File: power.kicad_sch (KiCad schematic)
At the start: 48 parts, among them J3 Barrel_Jack_Switch, Q10 RJK0355DSP, Q11 DMP3037LSS-13, Q8 2N7002, Q9 RJK0355DSP, U5 MIC2101, U6 NCP1117-3.3_SOT223

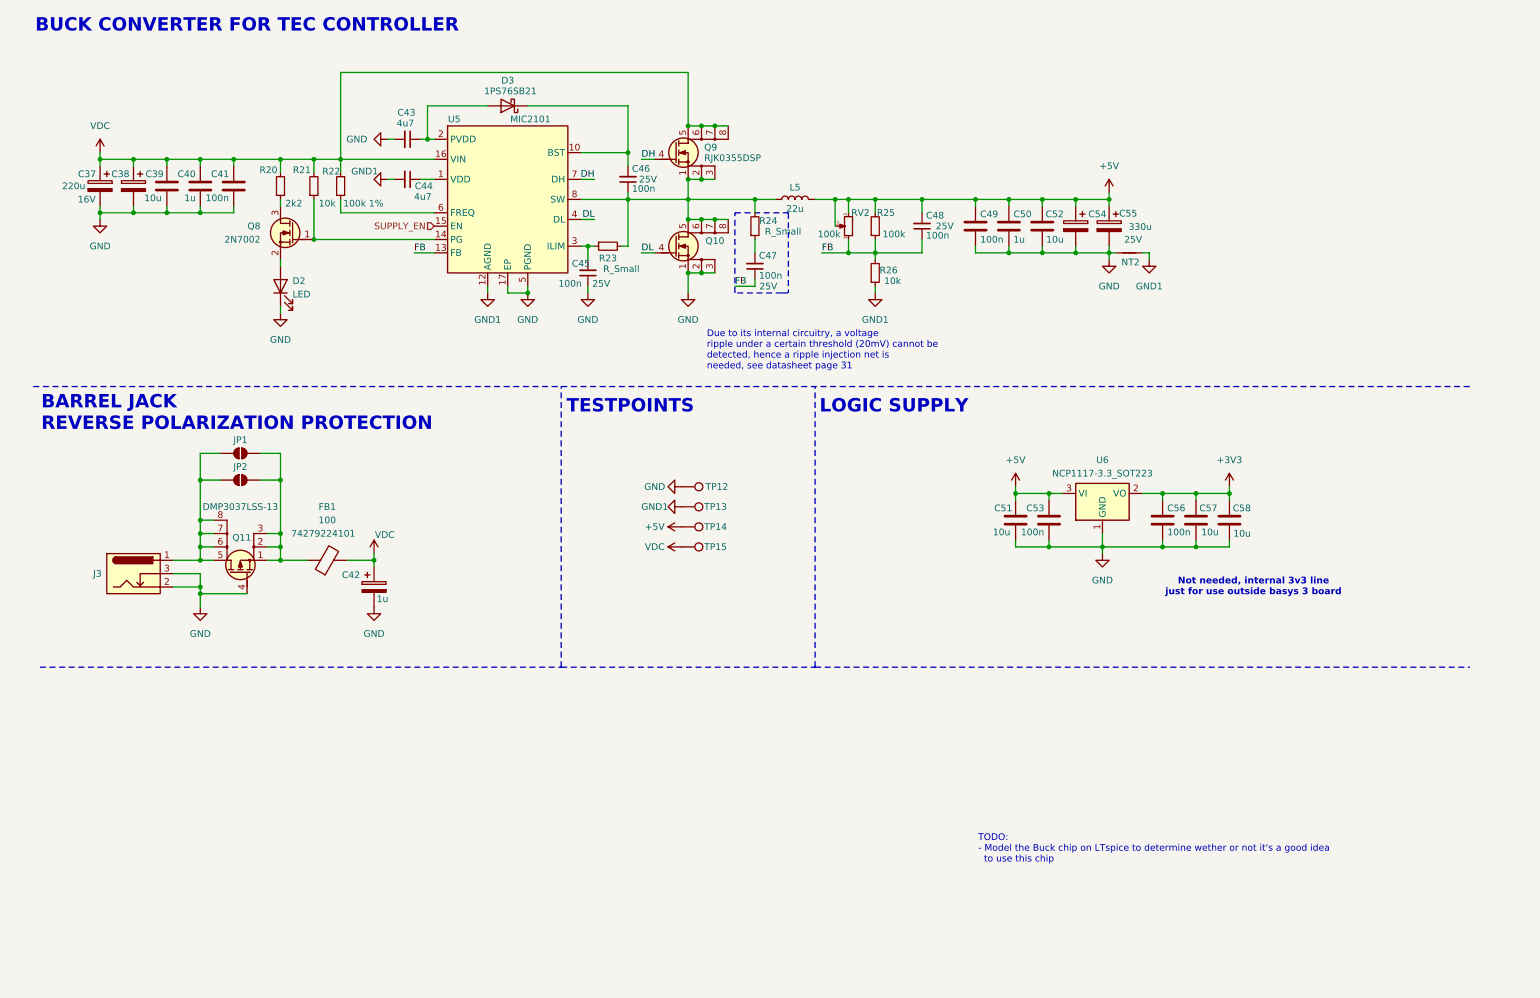
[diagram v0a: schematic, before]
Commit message: small schematic correction, structural changes to the 5V buck on the pcb
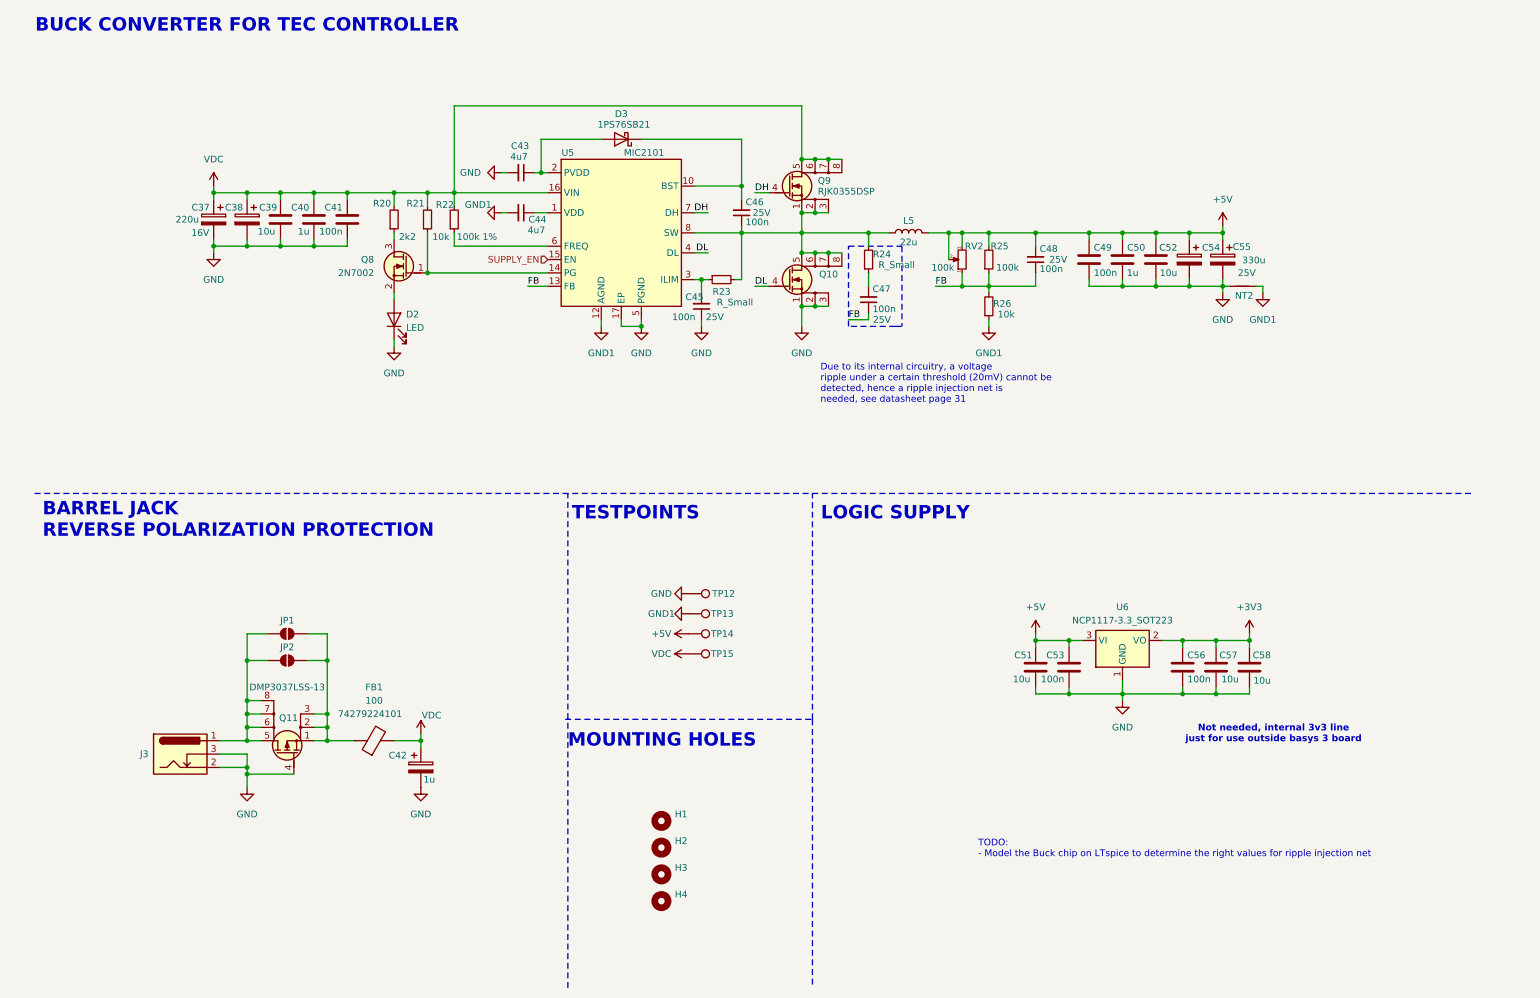
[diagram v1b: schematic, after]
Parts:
- added H1, H2, H3, H4: MountingHole, MountingHole:MountingHole_3.2mm_M3_ISO7380, symbol Mechanical:MountingHole
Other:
- note added: "MOUNTING HOLES"
- note added: "TODO: - Model the Buck chip on LTspice to determine the right values for ripple injection net"
- note removed: "TODO: - Model the Buck chip on LTspice to determine wether or not it's a good idea to use this chip"
- moved on the sheet: C37, C38, C39, C40, C41, C42, C43, C44, C45, C46, C47, C48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

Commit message: update PCB: fixed buck layout, concept layout for LD driver with LT3743
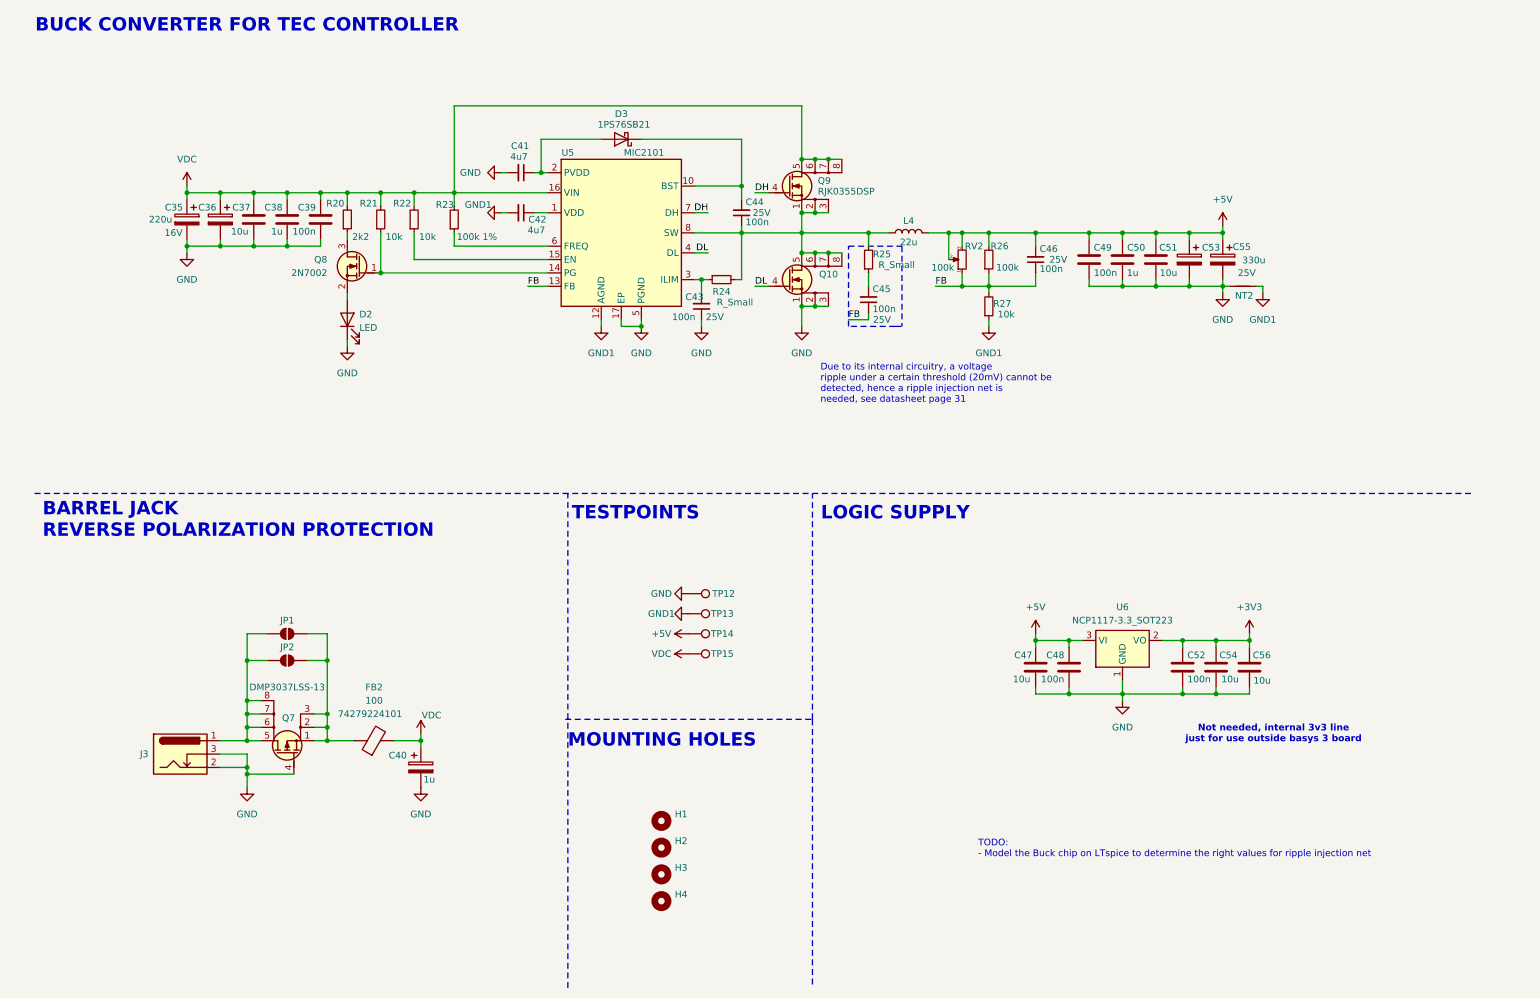
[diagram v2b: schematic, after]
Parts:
- added R22: 10k, Resistor_SMD:R_0603_1608Metric, symbol Device:R_Small
- TP13: footprint TestPoint:TestPoint_Pad_2.5x2.5mm -> TestPoint:TestPoint_Pad_1.0x1.0mm
- renumbered C37 to C35, C38 to C36, C39 to C37, C40 to C38, C41 to C39, C42 to C40, C43 to C41, C44 to C42, C45 to C43, C46 to C44, C47 to C45, C48 to C46, C51 to C47, C53 to C48, C52 to C51, C56 to C52, C54 to C53, C57 to C54, C58 to C56, FB1 to FB2, L5 to L4, Q11 to Q7, R22 to R23, R23 to R24, R24 to R25, R25 to R26, R26 to R27
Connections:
- net VDC: now also R22.2
- net SUPPLY_EN: no longer names the net of U5.15 (EN)
- net SUPPLY_EN: now also R22.1
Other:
- moved on the sheet: C35, C36, C37, C38, C39, D2, Q8, R20, R21

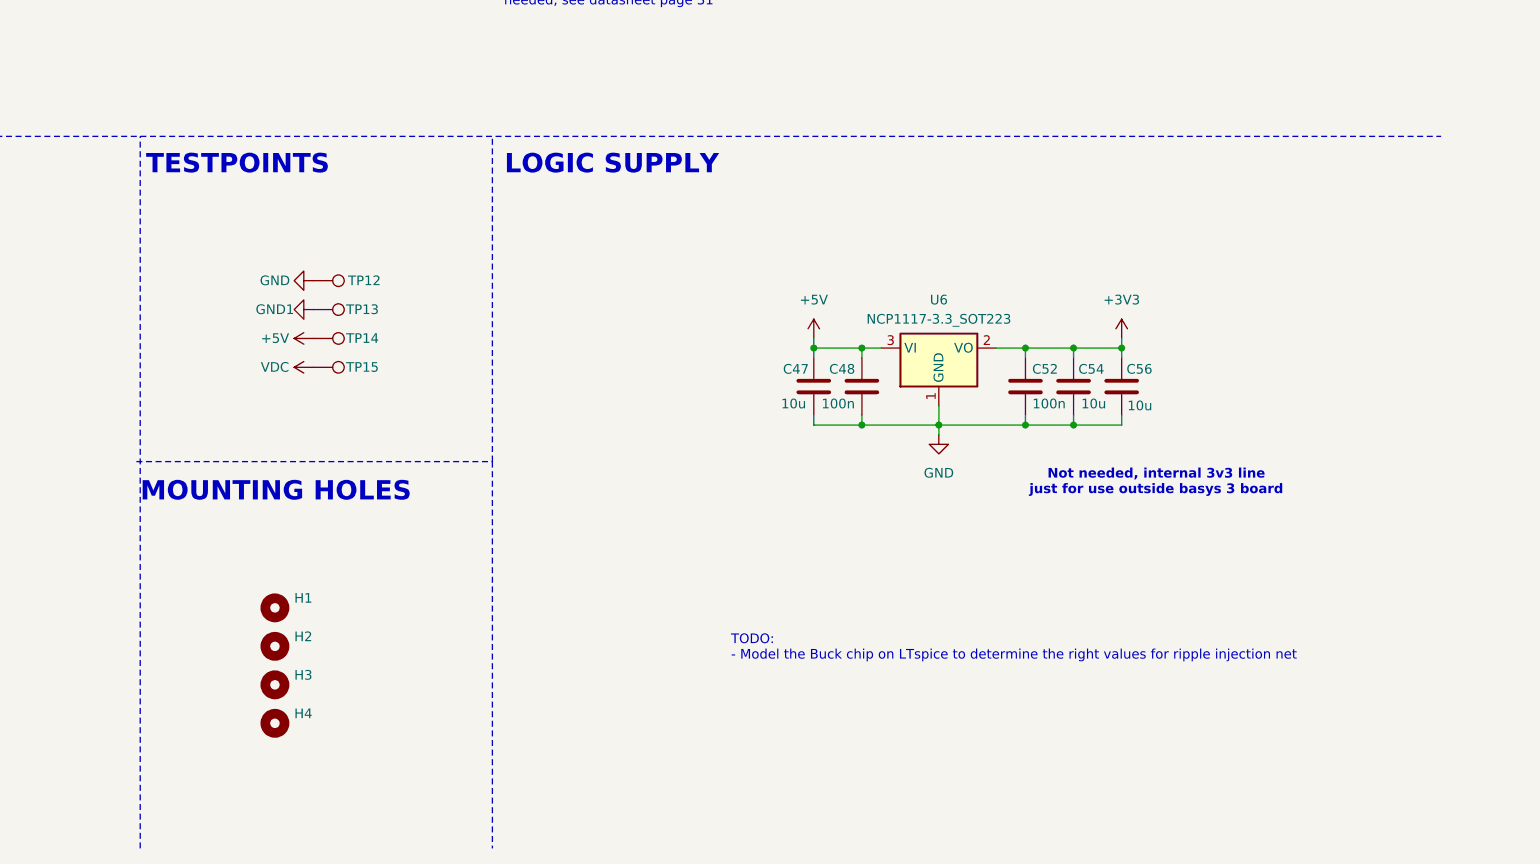
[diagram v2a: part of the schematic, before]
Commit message: Changed overall subsystem positions, TEC controller implemented, LD controller IC position to be reconsidered in order to have enough clearance after header connector is fully routed
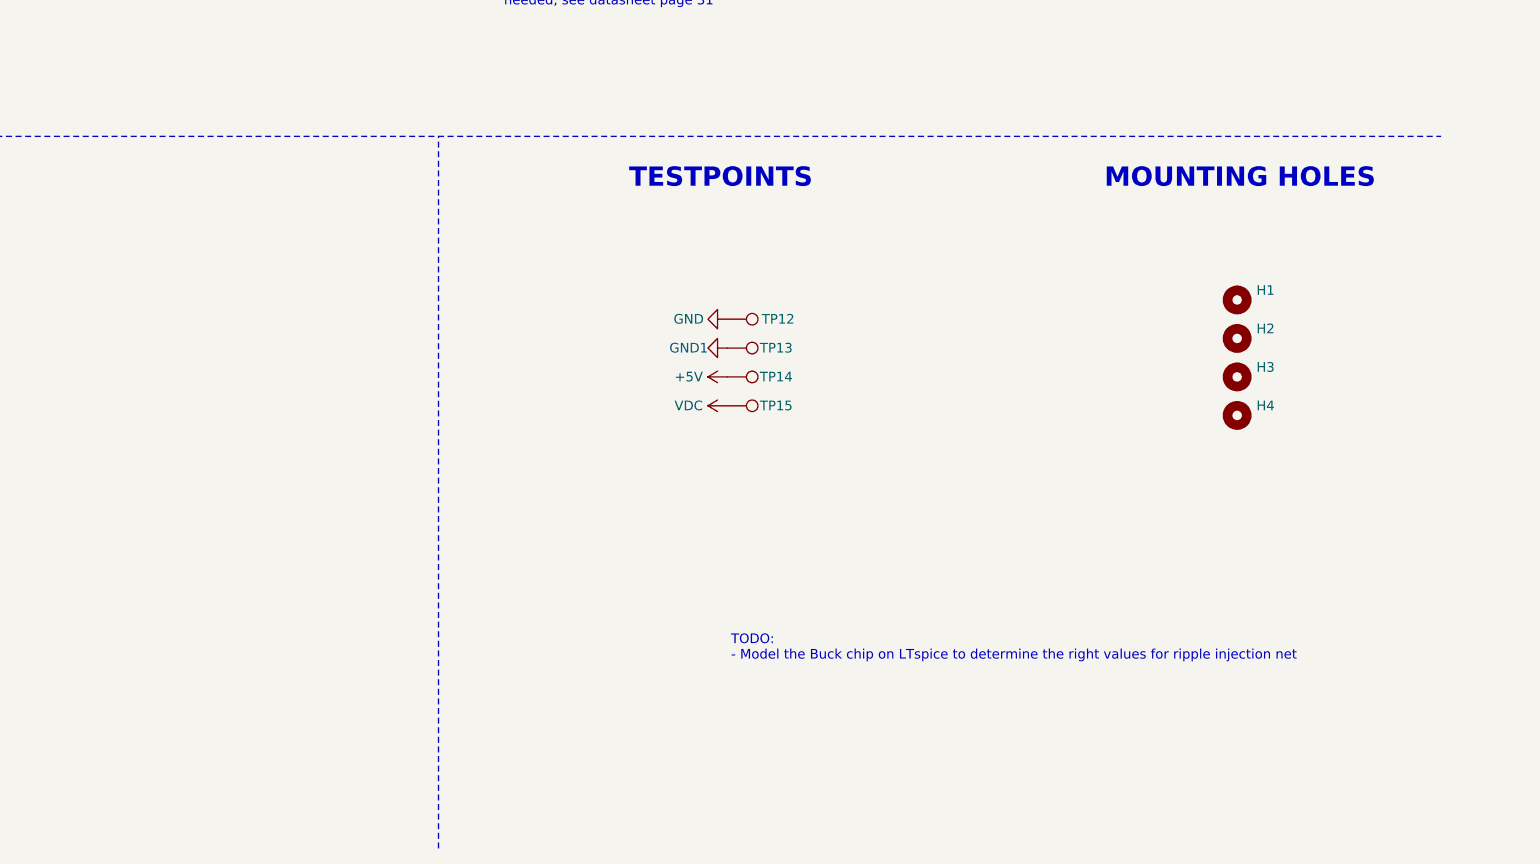
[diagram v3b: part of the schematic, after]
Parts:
- removed C47, C54, C56: 10u, Capacitor_SMD:C_0805_2012Metric, symbol Device:C
- removed C48, C52: 100n, Capacitor_SMD:C_0805_2012Metric, symbol Device:C
- removed U6: NCP1117-3.3_SOT223, Package_TO_SOT_SMD:SOT-223-3_TabPin2, symbol Regulator_Linear:NCP1117-3.3_SOT223
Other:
- note removed: "LOGIC SUPPLY"
- note removed: "Not needed, internal 3v3 line just for use outside basys 3 board"
- moved on the sheet: H1, H2, H3, H4, TP12, TP13, TP14, TP15

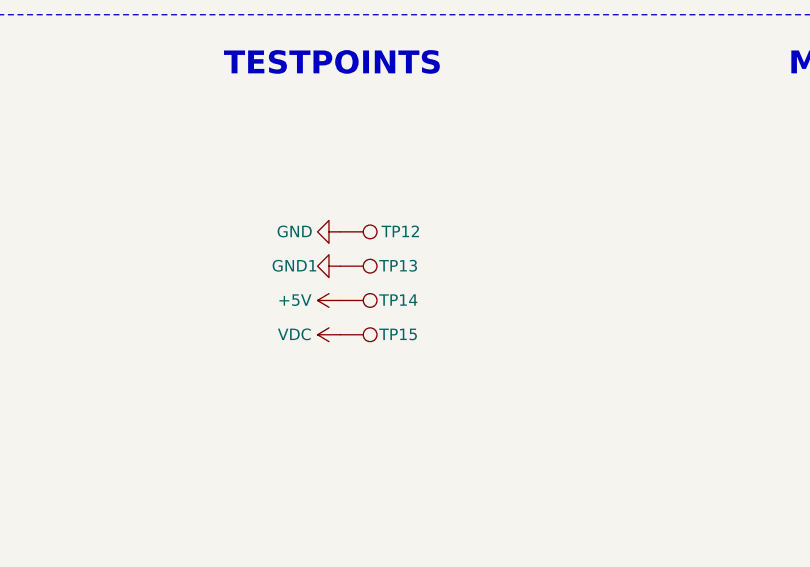
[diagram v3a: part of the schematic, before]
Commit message: PCB routing completed, started uniforming components for smaller BOM
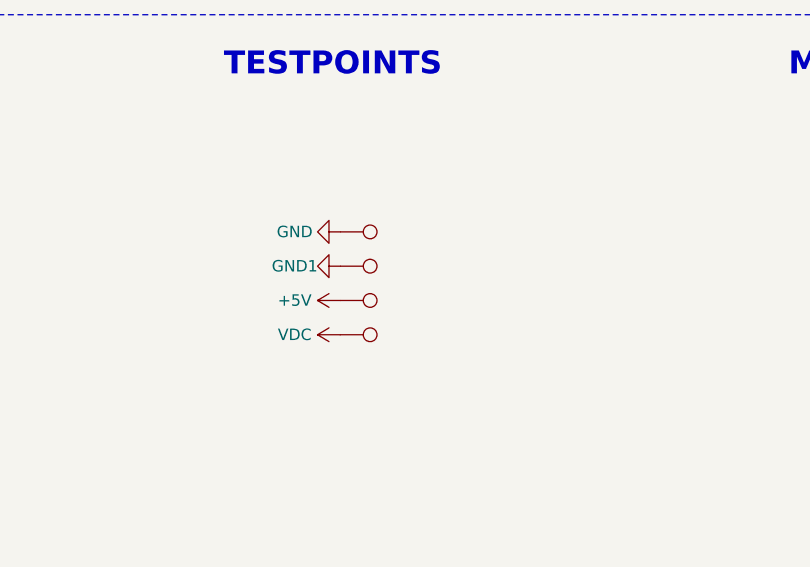
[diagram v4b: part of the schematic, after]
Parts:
- C37, C41, C42, C51: Voltage Rating 16V -> 25V
